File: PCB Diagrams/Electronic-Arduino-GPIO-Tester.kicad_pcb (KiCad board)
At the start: 2 copper layers, 109.2 x 61 mm, 49 parts, among them J2 Conn_01x02, J3 Conn_01x12, J4 Conn_01x08

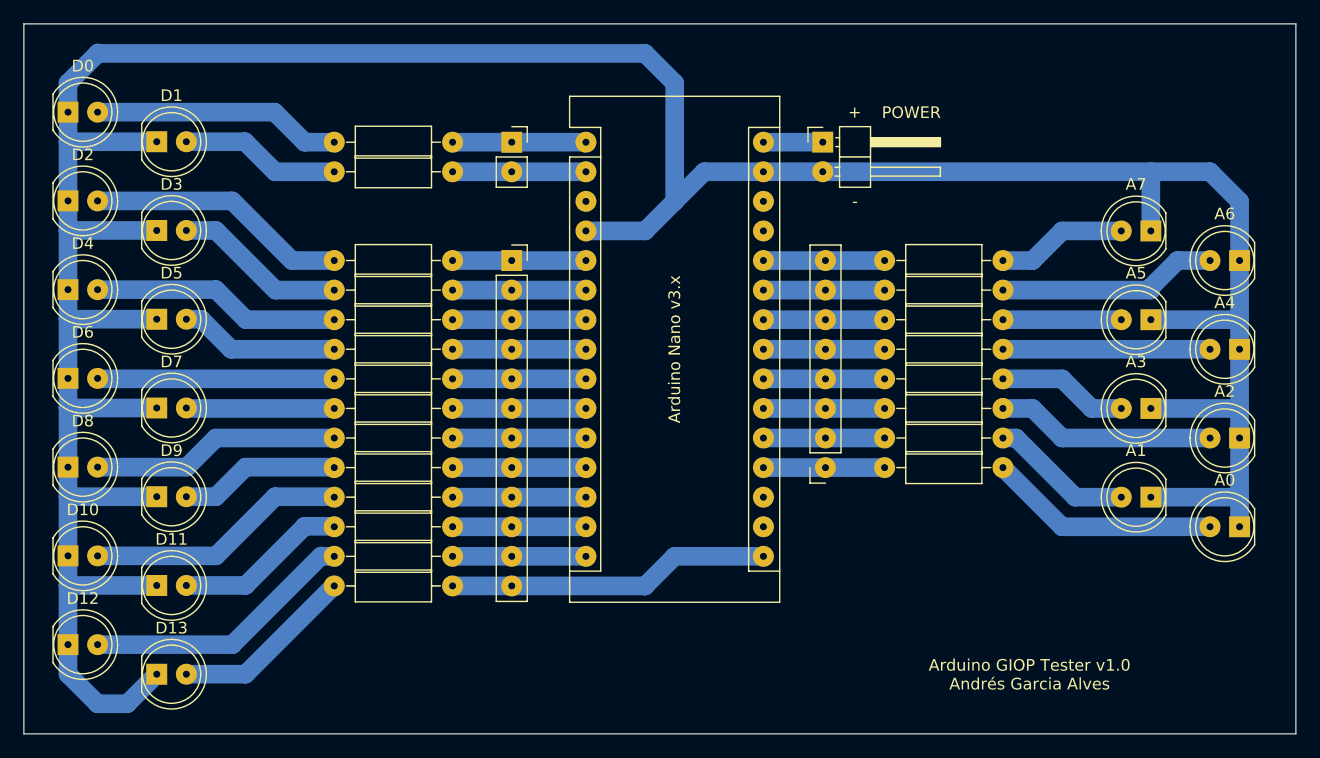
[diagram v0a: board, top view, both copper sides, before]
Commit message: pcb size optimization
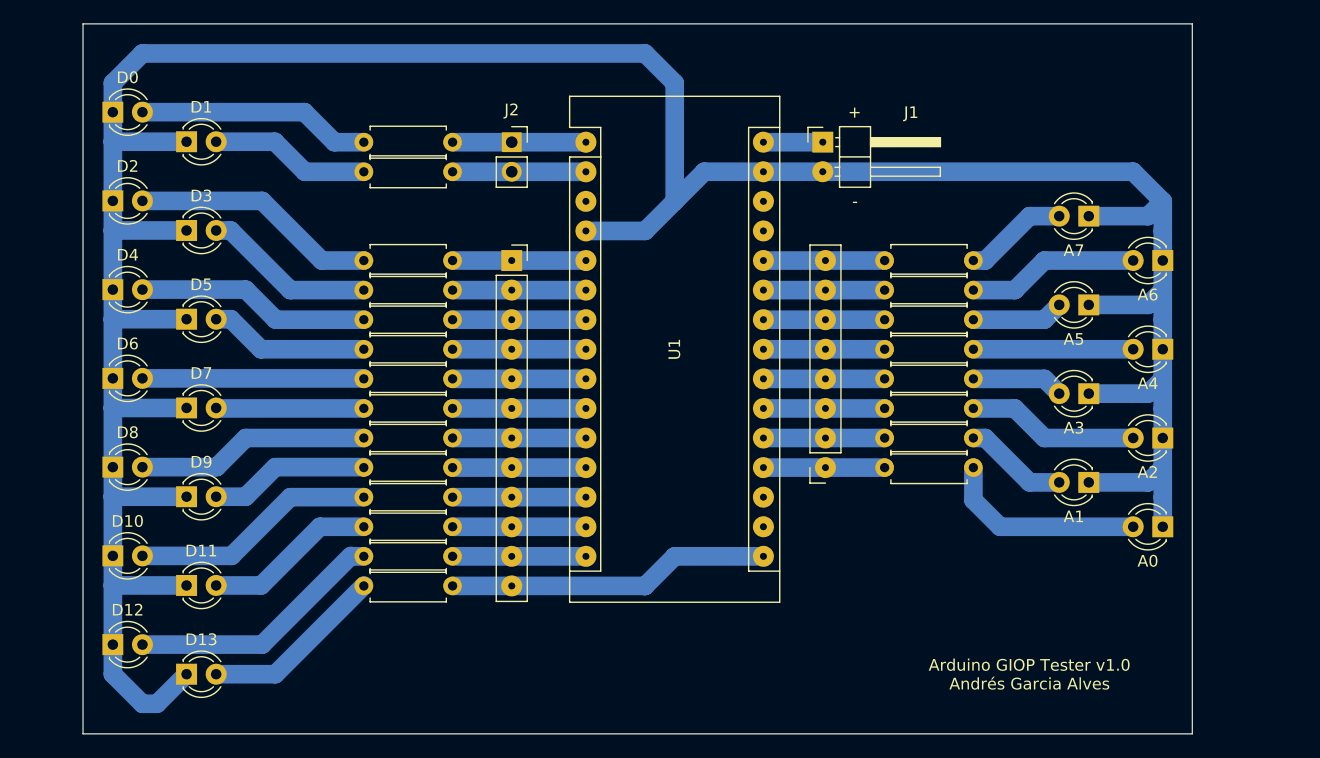
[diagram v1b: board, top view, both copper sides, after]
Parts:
- A0, A1, A2, A3, A4, A5, A6, A7, D0, D1, D10, D11, D12, D13, D2, D3, D4, D5, D6, D7, D8, D9: footprint LED_THT:LED_D5.0mm -> LED_THT:LED_D3.0mm
- R1: renamed from R2; value 2K -> 1K; footprint Resistor_THT:R_Axial_DIN0207_L6.3mm_D2.5mm_P10.16mm_Horizontal -> Resistor_THT:R_Axial_DIN0207_L6.3mm_D2.5mm_P7.62mm_Horizontal
- R10, R11, R12, R13, R14, R15, R16, R17, R18, R19, R20, R21, R22, R3, R4, R5, R6, R7, R8, R9: value 2K -> 1K; footprint Resistor_THT:R_Axial_DIN0207_L6.3mm_D2.5mm_P10.16mm_Horizontal -> Resistor_THT:R_Axial_DIN0207_L6.3mm_D2.5mm_P7.62mm_Horizontal
- R2: renamed from R1; value 2K -> 1K; footprint Resistor_THT:R_Axial_DIN0207_L6.3mm_D2.5mm_P10.16mm_Horizontal -> Resistor_THT:R_Axial_DIN0207_L6.3mm_D2.5mm_P7.62mm_Horizontal
- U1: renamed from Arduino Nano v3.x
- moved A0 6.60 mm to (148.6, 109.2)
- moved A2 6.60 mm to (148.6, 101.6)
- moved A4 6.60 mm to (148.6, 94.0)
- moved A6 6.60 mm to (148.6, 86.4)
- moved A1 5.48 mm to (142.2, 105.4)
- moved A3 5.48 mm to (142.2, 97.8)
- moved A5 5.48 mm to (142.2, 90.2)
- moved A7 5.48 mm to (142.2, 82.5)
- moved D0 3.85 mm to (58.4, 73.6)
- moved D10 3.85 mm to (58.4, 111.7)
- moved D12 3.85 mm to (58.4, 119.3)
- moved D2 3.85 mm to (58.4, 81.2)
- moved D4 3.85 mm to (58.4, 88.9)
- moved D6 3.85 mm to (58.4, 96.5)
- moved D8 3.85 mm to (58.4, 104.1)
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- renumbered POWER to J1
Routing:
- net GND: track 285.8 -> 265.8 mm
- net Net-(A6-Pad2): track 19.0 -> 14.8 mm
- net Net-(A2-Pad2): track 18.8 -> 14.8 mm
- net Net-(A4-Pad2): track 17.8 -> 13.7 mm
- net Net-(A1-Pad2): track 12.3 -> 8.95 mm
- net Net-(A3-Pad2): track 11.2 -> 7.90 mm
- net Net-(A0-Pad2): track 19.9 -> 17.5 mm
- net Net-(A7-Pad2): track 11.2 -> 8.95 mm
- net Net-(A5-Pad2): track 10.2 -> 7.90 mm
- net Net-(D10-Pad2): track 22.4 -> 21.1 mm
- net Net-(D6-Pad2): track 20.3 -> 19.0 mm
- net Net-(D4-Pad2): track 21.4 -> 20.1 mm
- net Net-(D8-Pad2): track 21.4 -> 20.1 mm
- net Net-(D2-Pad2): track 22.4 -> 21.2 mm
- net Net-(D0-Pad2): track 21.4 -> 20.1 mm
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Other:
- board size 109.2 x 61 mm -> 95.2 x 61 mm
